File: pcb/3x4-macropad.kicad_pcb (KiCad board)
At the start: 2 copper layers, 83.1 x 78.9 mm, 48 parts, among them SW1 SW_Push, SW10 SW_Push, SW11 SW_Push, SW12 SW_Push, SW2 SW_Push, SW3 SW_Push, SW4 SW_Push, SW5 SW_Push, SW6 SW_Push, SW7 SW_Push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

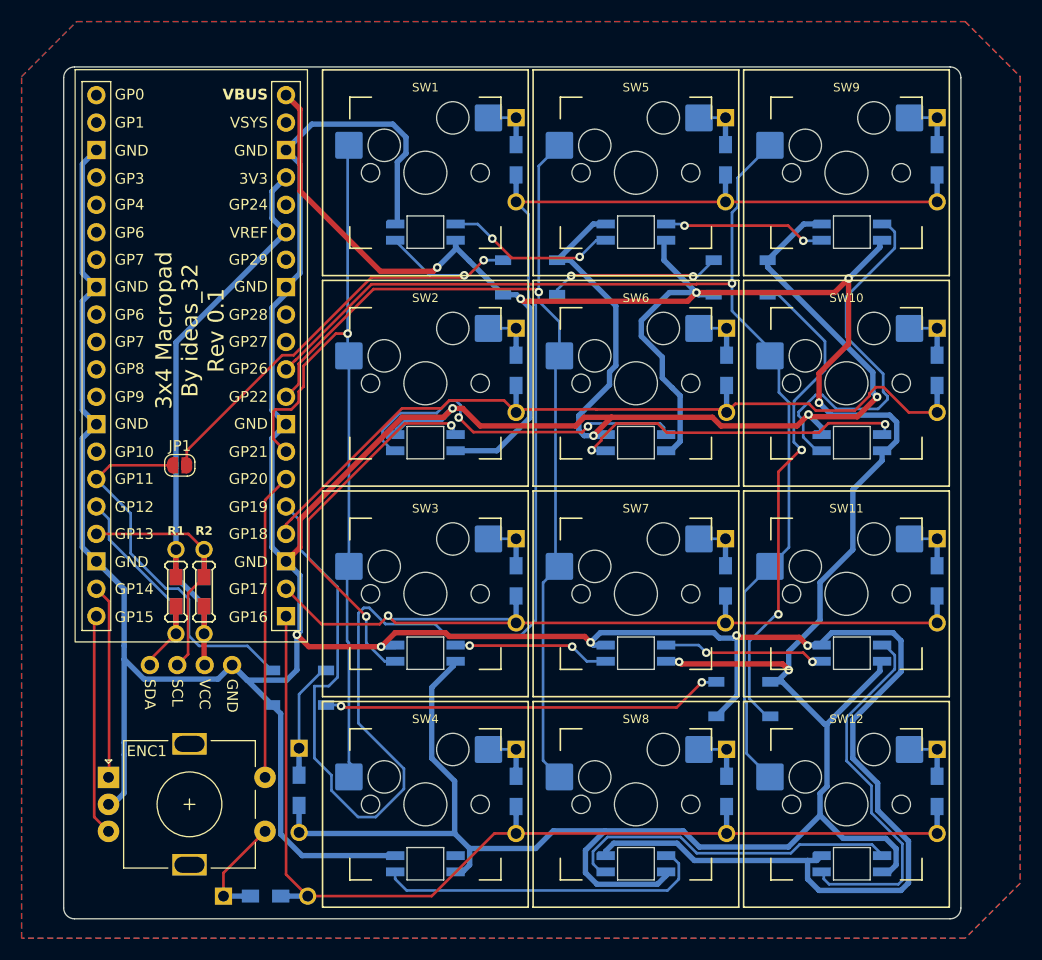
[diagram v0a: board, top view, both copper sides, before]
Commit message: Init rp2040 on board
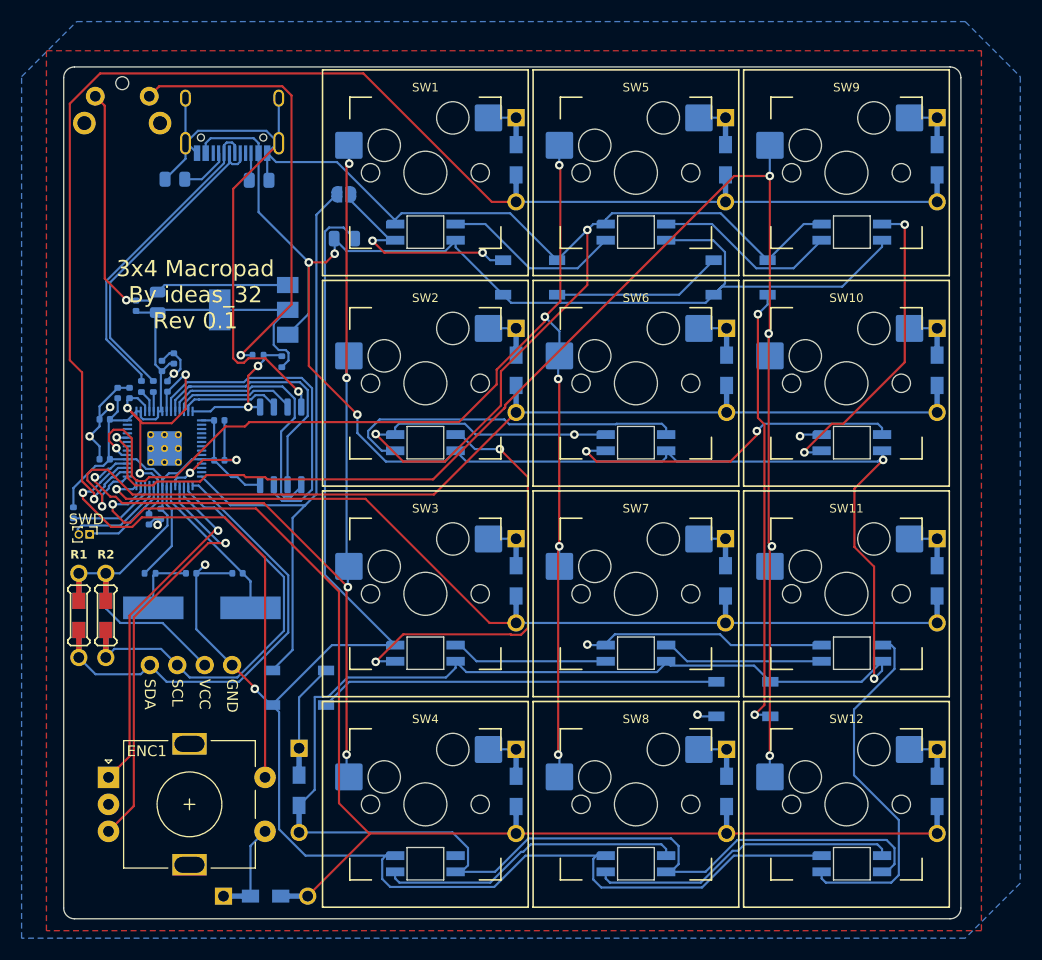
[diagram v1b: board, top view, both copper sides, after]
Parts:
- added C1: 10u, Capacitor_SMD:C_0805_2012Metric, B.Cu at (153.5, 47.1)
- added C10: 1u, Capacitor_SMD:C_0402_1005Metric, B.Cu at (137.1, 60.8)
- added C11: 100n, Capacitor_SMD:C_0402_1005Metric, B.Cu at (135.4, 73.1)
- added C12: 100n, Capacitor_SMD:C_0402_1005Metric, B.Cu at (133.6, 61.4)
- added C13: 100n, Capacitor_SMD:C_0402_1005Metric, B.Cu at (134.2, 53.3)
- added C14: 27pF, Capacitor_SMD:C_0402_1005Metric, B.Cu at (139.3, 78.1)
- added C15: 27pF, Capacitor_SMD:C_0402_1005Metric, B.Cu at (143.6, 78.1)
- added C16: 10u, Capacitor_SMD:C_0805_2012Metric, B.Cu at (136.2, 53.0)
- added C2: 1u, Capacitor_SMD:C_0402_1005Metric, B.Cu at (132.5, 61.4)
- added C3: 100n, Capacitor_SMD:C_0402_1005Metric, B.Cu at (136.5, 72.6)
- added C4: 100n, Capacitor_SMD:C_0402_1005Metric, B.Cu at (141.9, 63.9)
- added C5: 100n, Capacitor_SMD:C_0402_1005Metric, B.Cu at (136.6, 58.9)
- added C6: 100n, Capacitor_SMD:C_0402_1005Metric, B.Cu at (141.9, 67.6)
- added C7: 100n, Capacitor_SMD:C_0402_1005Metric, B.Cu at (131.3, 63.8)
- added C8: 100n, Capacitor_SMD:C_0402_1005Metric, B.Cu at (131.3, 67.5)
- added C9: 100n, Capacitor_SMD:C_0402_1005Metric, B.Cu at (137.7, 58.2)
- added J2: Conn_01x02, Keebio-Parts:SW_Tactile_SPST_Angled_MJTP1117, B.Cu at (135.4, 33.9)
- added J3: SWD, Connector_PinHeader_1.00mm:PinHeader_1x02_P1.00mm_Vertical, F.Cu at (129.9, 74.5)
- added J4: USB_C_Receptacle_USB2.0, Connector_USB:USB_C_Receptacle_HRO_TYPE-C-31-M-12, B.Cu at (143.1, 35.1)
- added R10: 1k, Resistor_SMD:R_0402_1005Metric, B.Cu at (128.4, 72.5)
- added R3: 5k1, Resistor_SMD:R_0805_2012Metric, B.Cu at (137.8, 41.6)
- added R4: 5k1, Resistor_SMD:R_0805_2012Metric, B.Cu at (145.6, 41.7)
- added R5: 27.4, Resistor_SMD:R_0402_1005Metric, B.Cu at (135.8, 60.8)
- added R6: 27.4, Resistor_SMD:R_0402_1005Metric, B.Cu at (134.7, 60.8)
- added R7: 1k, Resistor_SMD:R_0402_1005Metric, B.Cu at (145.5, 57.9)
- added R8: DNF(10k), Resistor_SMD:R_0402_1005Metric, B.Cu at (147.7, 58.5)
- added R9: 1k, Resistor_SMD:R_0402_1005Metric, B.Cu at (135.5, 78.1)
- added U2: NCP1117-3.3_SOT223, Package_TO_SOT_SMD:SOT-223-3_TabPin2, B.Cu at (145.1, 53.7)
- added U3: W25Q32JVSS, Package_SO:SOIC-8_5.23x5.23mm_P1.27mm, B.Cu at (147.6, 66.3)
- added Y1: ABLS_12.000MHZ-B4-T, RP2040_minimal:Crystal_SMD_HC49-US, B.Cu at (140.3, 81.3)
- JP1: moved to B.Cu
- U1: value WeAct-RP2040-Pico -> RP2040; footprint WeAct-RP2040-Pico:WeAct-RP2040-Pico -> RP2040_minimal:RP2040-QFN-56; moved to B.Cu
- moved JP1 29.3 mm to (153.4, 43.0)
- moved R2 9.36 mm to (131.4, 82.0), turned to -90 degrees
- moved R1 9.26 mm to (128.9, 82.0)
- moved U1 8.93 mm to (136.8, 66.5), turned to 180 degrees
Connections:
- ENC1 pad C: GND -> GND1
- LED1 pad 3: GND -> GND1
- LED10 pad 3: GND -> GND1
- LED11 pad 3: GND -> GND1
- LED12 pad 3: GND -> GND1
- LED13 pad 3: GND -> GND1
- LED14 pad 3: GND -> GND1
- LED15 pad 3: GND -> GND1
- LED16 pad 3: GND -> GND1
- LED2 pad 3: GND -> GND1
- LED3 pad 3: GND -> GND1
- LED4 pad 3: GND -> GND1
- LED5 pad 3: GND -> GND1
- LED6 pad 3: GND -> GND1
- LED7 pad 3: GND -> GND1
- LED8 pad 3: GND -> GND1
- LED9 pad 3: GND -> GND1
- OLED1 pad 1: GND -> GND1
- OLED1 pad 2: VCC -> +3V3
- R1 pad 2: VCC -> +3V3
- R2 pad 2: VCC -> +3V3
- U1 pad 1: unconnected-(U1-GP0-Pad1) -> +3V3
- U1 pad 10: unconnected-(U1-GP7-Pad10) -> +3V3
- U1 pad 13: GND -> unconnected-(U1-GPIO10-Pad13)
- U1 pad 14: unconnected-(U1-GP10-Pad14) -> RGB
- U1 pad 15: RGB -> OLED_SDA
- U1 pad 16: OLED_SDA -> OLED_SCL
- U1 pad 17: OLED_SCL -> ENC_A
- U1 pad 18: GND -> ENC_B
- U1 pad 19: ENC_A -> GND1
- U1 pad 20: ENC_B -> Net-(U1-XIN)
- U1 pad 21: ROW3 -> Net-(U1-XOUT)
- U1 pad 22: ROW2 -> +3V3
- U1 pad 23: GND -> +1V1
- U1 pad 24: ROW1 -> SWCLK
- U1 pad 25: ROW0 -> SWD
- U1 pad 26: COL0 -> Net-(U1-RUN)
- U1 pad 27: COL1 -> ROW3
- U1 pad 28: GND -> ROW2
- U1 pad 29: COL2 -> ROW1
- U1 pad 3: GND -> unconnected-(U1-GPIO1-Pad3)
- U1 pad 30: COL3 -> ROW0
- U1 pad 31: unconnected-(U1-GP27-Pad31) -> COL0
- U1 pad 32: unconnected-(U1-GP28-Pad32) -> COL1
- U1 pad 33: GND -> +3V3
- U1 pad 34: unconnected-(U1-GP29-Pad34) -> COL2
- U1 pad 35: VCC -> unconnected-(U1-GPIO23-Pad35)
- U1 pad 37: VCC -> unconnected-(U1-GPIO25-Pad37)
- U1 pad 38: GND -> COL3
- U1 pad 40: VBUS -> unconnected-(U1-GPIO28_ADC2-Pad40)
- U1 pad 8: GND -> unconnected-(U1-GPIO6-Pad8)
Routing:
- net GND: track 444.5 -> 0.00 mm, vias 9 -> 0
- net GND1: track 0.00 -> 420.6 mm, vias 0 -> 16
- net +3V3: track 0.00 -> 98.6 mm
- net VCC: track 46.5 -> 0.00 mm
- net USB_BOOT: track 0.00 -> 41.0 mm, vias 0 -> 1
- net COL3: track 107.6 -> 139.9 mm, vias 1 -> 5
- net ROW0: track 158.4 -> 128.3 mm, vias 0 -> 1
- net USB_D+: track 0.00 -> 30.1 mm
- net QSPI_SD3: track 0.00 -> 29.9 mm
- net USB_D-: track 0.00 -> 29.6 mm
- net +1V1: track 0.00 -> 29.1 mm, vias 0 -> 3
- net COL2: track 89.4 -> 116.4 mm, vias 1 -> 6
- net VBUS: track 302.8 -> 329.2 mm, vias 7 -> 5
- net Net-(JP1-B): track 45.4 -> 20.1 mm
- net OLED_SDA: track 16.2 -> 40.5 mm
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- added copper zone on B.Cu, net +3V3
- added copper zone on F.Cu, net GND1
- removed copper zone on B.Cu, net GND
- removed copper zone on F.Cu, net GND
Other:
- board text added: "R2"
- board text removed: "COL0"
- board text removed: "COL1"
- board text removed: "COL2"
- board text removed: "COL3"
- board text removed: "ENC A"
- board text removed: "ENC B"
- board text removed: "GND"
- board text removed: "Pins not labeled are unused"
- board text removed: "RGB"
- board text removed: "ROW0"
- board text removed: "ROW1"
- board text removed: "ROW2"
- board text removed: "ROW3"
- board text removed: "SCL"
- board text removed: "SDA"
- board text removed: "VBUS"
- board text removed: "VCC"
